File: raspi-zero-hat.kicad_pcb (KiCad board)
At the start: 2 copper layers, 65 x 30 mm, 12 parts, among them J1 Screw_Terminal_01x02, J2 Screw_Terminal_01x03, K1 G5LE-1, P1 Conn_02x20_Odd_Even

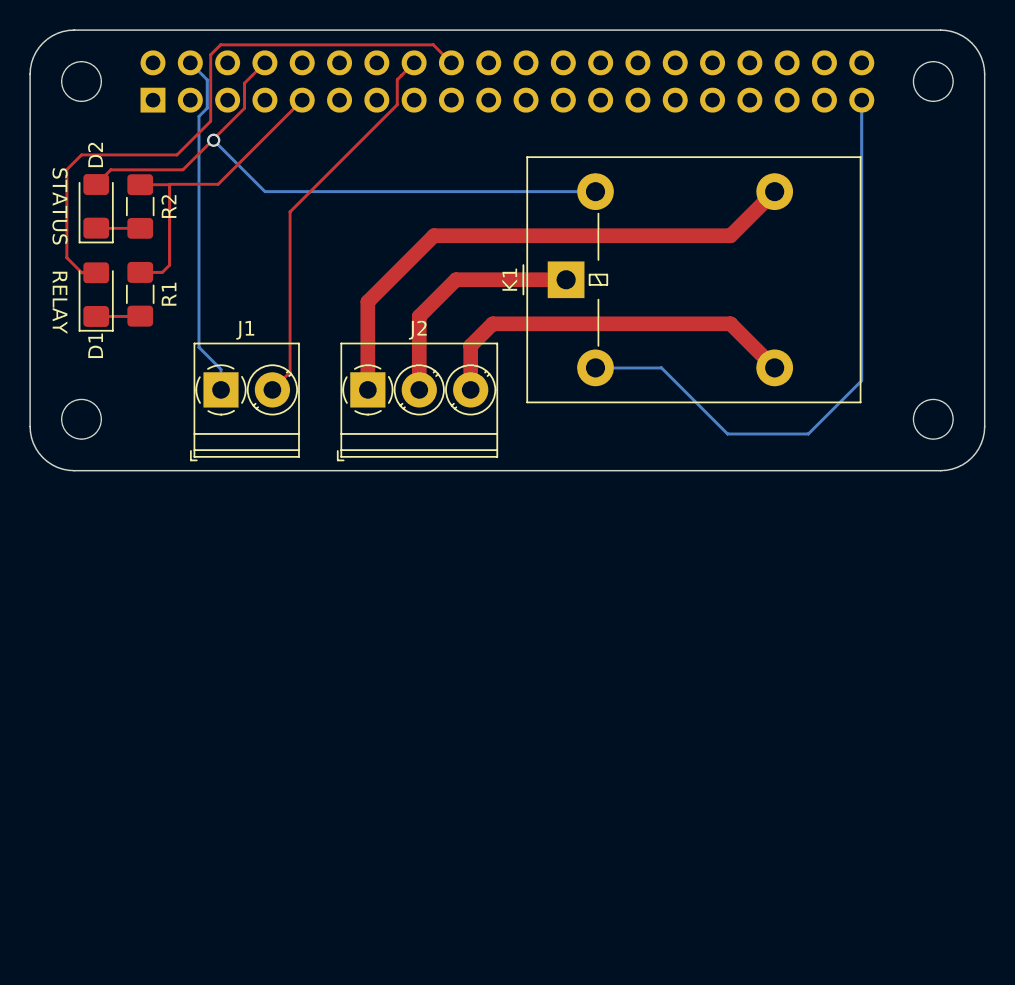
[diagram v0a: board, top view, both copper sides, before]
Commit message: added NPN for relay drive. duplicated PCB w/ perforations.
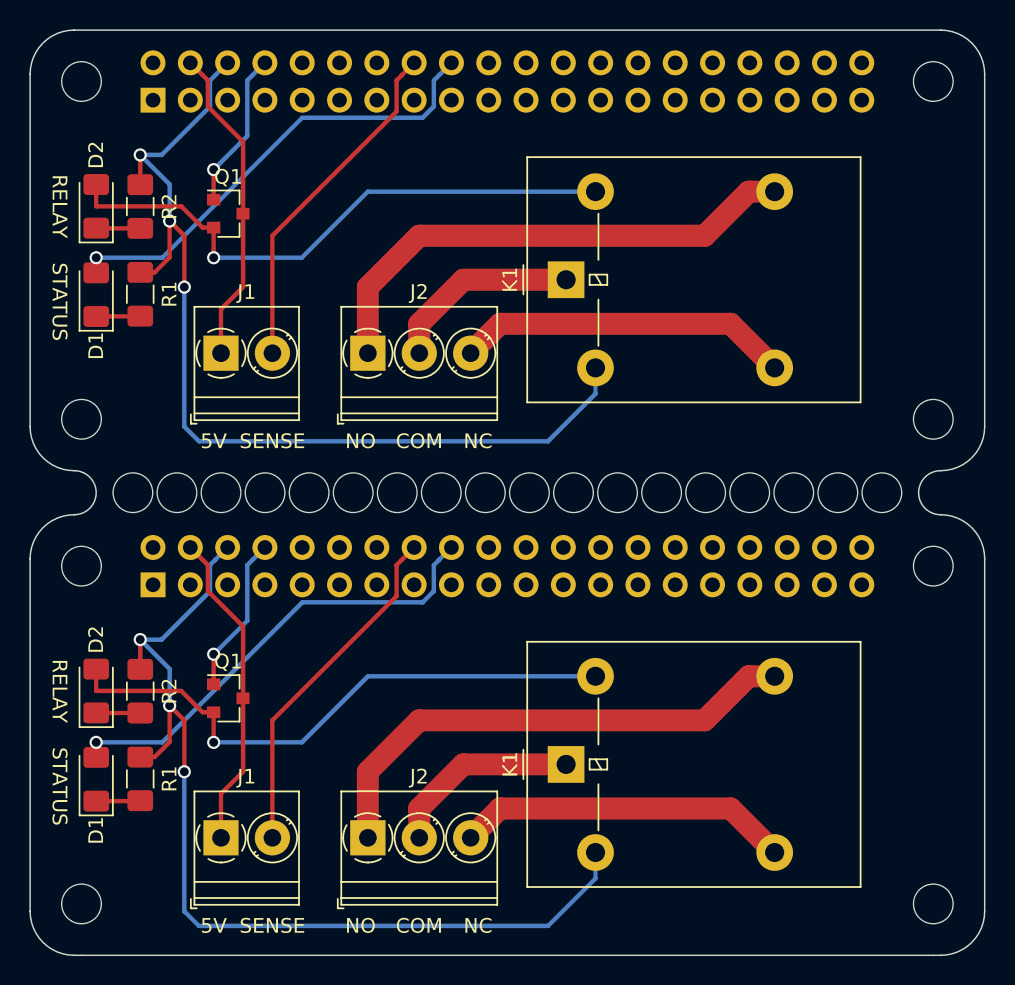
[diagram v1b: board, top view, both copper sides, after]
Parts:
- added D1: LED, LED_SMD:LED_1206_3216Metric_Pad1.42x1.75mm_HandSolder, F.Cu at (204.5, 171.0)
- added D2: LED, LED_SMD:LED_1206_3216Metric_Pad1.42x1.75mm_HandSolder, F.Cu at (204.5, 165.0)
- added J1: Screw_Terminal_01x02, TerminalBlock_Phoenix:TerminalBlock_Phoenix_PT-1,5-2-3.5-H_1x02_P3.50mm_Horizontal, F.Cu at (213.0, 175.0)
- added J2: Screw_Terminal_01x03, TerminalBlock_Phoenix:TerminalBlock_Phoenix_PT-1,5-3-3.5-H_1x03_P3.50mm_Horizontal, F.Cu at (223.0, 175.0)
- added K1: G5LE-1, Relay_THT:Relay_SPDT_Omron-G5LE-1, F.Cu at (236.5, 170.0)
- added MK1: M2.5, MountingHole:MountingHole_2.7mm_M2.5, F.Cu at (203.5, 156.5)
- added MK1: M2.5, MountingHole:MountingHole_2.7mm_M2.5, F.Cu at (234.0, 151.5)
- added MK1: M2.5, MountingHole:MountingHole_2.7mm_M2.5, F.Cu at (228.0, 151.5)
- added MK1: M2.5, MountingHole:MountingHole_2.7mm_M2.5, F.Cu at (225.0, 151.5)
- added MK1: M2.5, MountingHole:MountingHole_2.7mm_M2.5, F.Cu at (231.0, 151.5)
- added MK1: M2.5, MountingHole:MountingHole_2.7mm_M2.5, F.Cu at (222.0, 151.5)
- added MK1: M2.5, MountingHole:MountingHole_2.7mm_M2.5, F.Cu at (219.0, 151.5)
- added MK1: M2.5, MountingHole:MountingHole_2.7mm_M2.5, F.Cu at (216.0, 151.5)
- added MK1: M2.5, MountingHole:MountingHole_2.7mm_M2.5, F.Cu at (213.0, 151.5)
- added MK1: M2.5, MountingHole:MountingHole_2.7mm_M2.5, F.Cu at (210.0, 151.5)
- added MK1: M2.5, MountingHole:MountingHole_2.7mm_M2.5, F.Cu at (207.0, 151.5)
- added MK1: M2.5, MountingHole:MountingHole_2.7mm_M2.5, F.Cu at (258.0, 151.5)
- added MK1: M2.5, MountingHole:MountingHole_2.7mm_M2.5, F.Cu at (252.0, 151.5)
- added MK1: M2.5, MountingHole:MountingHole_2.7mm_M2.5, F.Cu at (255.0, 151.5)
- added MK1: M2.5, MountingHole:MountingHole_2.7mm_M2.5, F.Cu at (237.0, 151.5)
- added MK1: M2.5, MountingHole:MountingHole_2.7mm_M2.5, F.Cu at (243.0, 151.5)
- added MK1: M2.5, MountingHole:MountingHole_2.7mm_M2.5, F.Cu at (249.0, 151.5)
- added MK1: M2.5, MountingHole:MountingHole_2.7mm_M2.5, F.Cu at (246.0, 151.5)
- added MK1: M2.5, MountingHole:MountingHole_2.7mm_M2.5, F.Cu at (240.0, 151.5)
- added MK2: M2.5, MountingHole:MountingHole_2.7mm_M2.5, F.Cu at (261.5, 156.5)
- added MK3: M2.5, MountingHole:MountingHole_2.7mm_M2.5, F.Cu at (203.5, 179.5)
- added MK4: M2.5, MountingHole:MountingHole_2.7mm_M2.5, F.Cu at (261.5, 179.5)
- added P1: Conn_02x20_Odd_Even, Connector_PinSocket_2.54mm:PinSocket_2x20_P2.54mm_Vertical, B.Cu at (208.4, 157.8)
- added Q1: MMBT3904, Package_TO_SOT_SMD:SOT-23, F.Cu at (213.5, 165.5)
- added Q1: MMBT3904, Package_TO_SOT_SMD:SOT-23, F.Cu at (213.5, 132.5)
- added R1: R, Resistor_SMD:R_1206_3216Metric_Pad1.42x1.75mm_HandSolder, F.Cu at (207.5, 171.0)
- added R2: R, Resistor_SMD:R_1206_3216Metric_Pad1.42x1.75mm_HandSolder, F.Cu at (207.5, 165.0)
- moved J1 2.50 mm to (213.0, 142.0)
- moved J2 2.50 mm to (223.0, 142.0)
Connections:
- D2 pad 2: /GPIO14(TXD0) -> Net-(D2-Pad2)
- K1 pad 5: /GPIO14(TXD0) -> Net-(D2-Pad2)
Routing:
- net Net-(D2-Pad2): track 0.00 -> 80.0 mm, vias 0 -> 2
- net GND: track 61.7 -> 135.6 mm, vias 0 -> 6
- net Net-(J2-Pad1): track 36.8 -> 69.8 mm
- net /GPIO24(GEN5): track 41.3 -> 63.5 mm, vias 0 -> 2
- net /GPIO14(TXD0): track 43.4 -> 21.5 mm, vias 1 -> 2
- net /GPIO23(GEN4): track 26.3 -> 47.5 mm
- net +5V: track 23.6 -> 43.8 mm
- net Net-(J2-Pad3): track 25.6 -> 45.5 mm
- net Net-(J2-Pad2): track 16.0 -> 26.5 mm
- net Net-(D1-Pad1): track 3.01 -> 6.02 mm
- net Net-(D2-Pad1): track 3.01 -> 6.01 mm
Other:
- board size 65 x 30 mm -> 65 x 63 mm
- net class Default: trace_width 0.2 -> 0.3
- net class Power: trace_width 1 -> 1.5
- board text added: "5V"
- board text added: "COM"
- board text added: "NC"
- board text added: "NO"
- board text added: "SENSE"
